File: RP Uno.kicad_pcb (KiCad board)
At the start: 2 copper layers, 68.6 x 53.3 mm, 73 parts, among them J1 USB_B, J2 Conn_01x08, J3 Conn_01x06, J4 Conn_01x10, J5 Conn_01x08, J6 Barrel_Jack_Switch, J7 ICSP, J8 SWD, Q1 FDN340P, Q2 FDN340P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

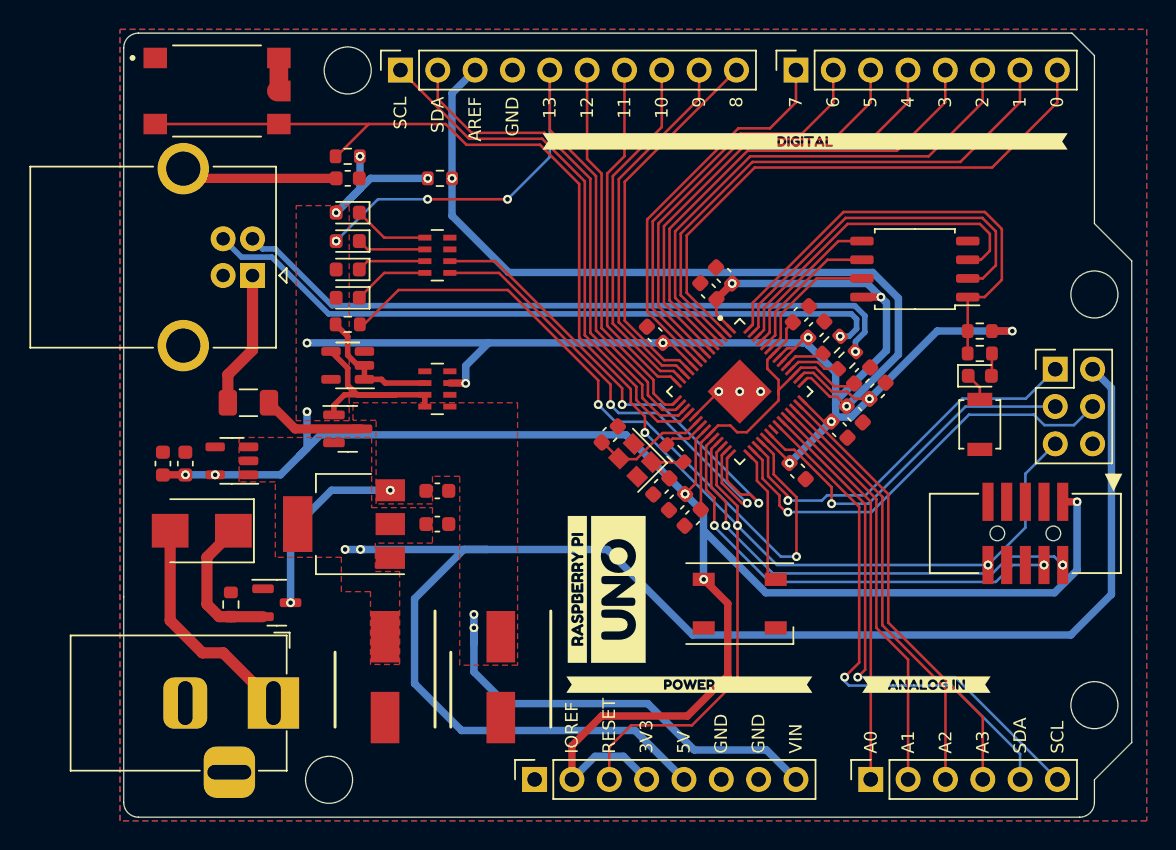
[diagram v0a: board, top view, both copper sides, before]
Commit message: Pinout changes and silkscreen additions
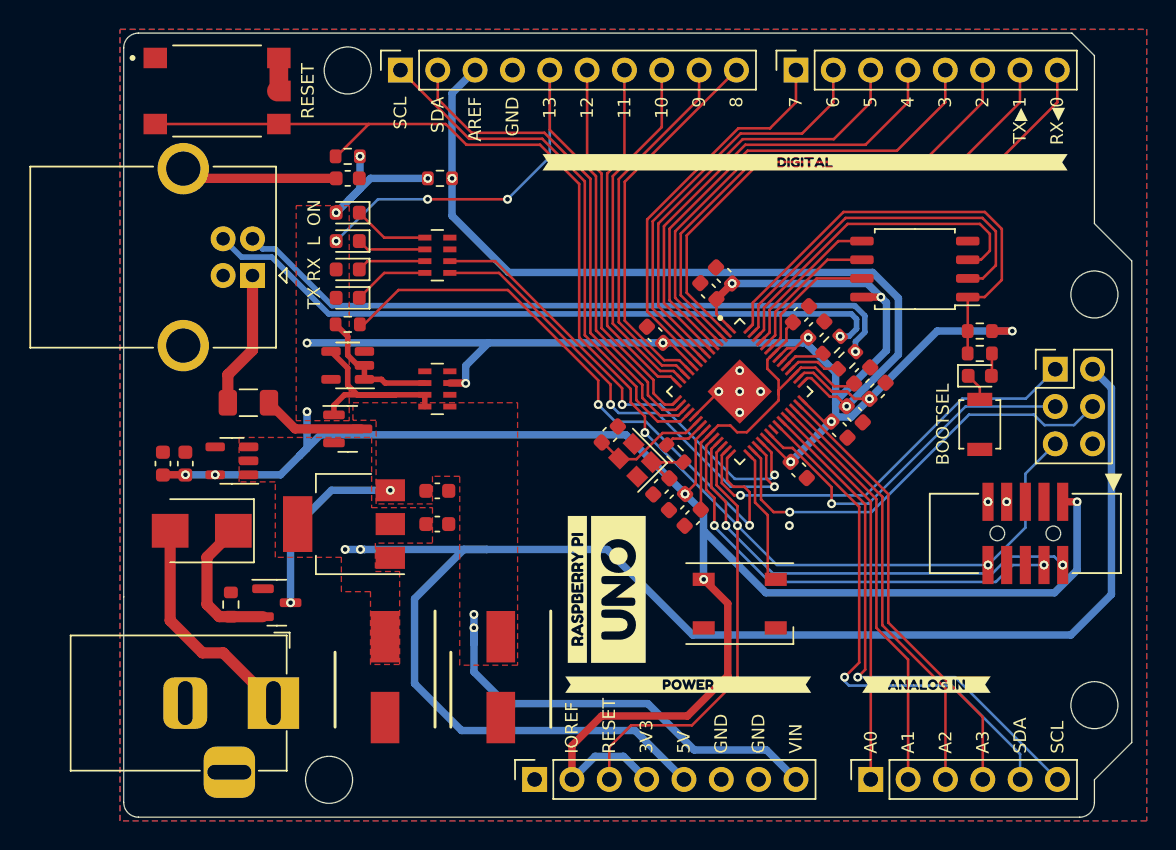
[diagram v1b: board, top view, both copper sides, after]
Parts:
- moved kibuzzard-639FD3EE 1.42 mm to (159.6, 90.1)
- moved C5 0.11 mm to (159.2, 111.0)
- moved kibuzzard-639FD42A 0.08 mm to (151.7, 125.6)
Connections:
- U1 pad 27: /TXLED -> /MISO
- U1 pad 28: /RXLED -> /USB_HOSTEN
- U1 pad 31: /MISO -> /TXLED
- U1 pad 32: /USB_HOSTEN -> /RXLED
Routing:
- net /USB_HOSTEN: track 47.7 -> 40.8 mm
- net /MISO: track 26.5 -> 29.0 mm
- net /RXLED: track 33.2 -> 31.6 mm
- net GND: vias 3 -> 8
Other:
- board text added: "BOOTSEL"
- board text added: "L"
- board text added: "ON"
- board text added: "RX"
- board text added: "RX◀0"
- board text added: "TX"
- board text added: "TX▶1"
- board text removed: "0"
- board text removed: "1"
